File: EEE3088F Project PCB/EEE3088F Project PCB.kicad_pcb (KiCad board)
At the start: 2 copper layers, 80 x 54.9 mm, 76 parts, among them IC1 74LVC1G04SE-7, J1 JST PH 2.00mm connector, SW1 SS-12D10L3, U1 DRV8833PWR, U10 LM7805L-TF3-T, U11 TC4056A., U2 DRV8833PWPR, U3 INA219AxD, U4 CH224K, U6 MIC5504-1.2YM5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

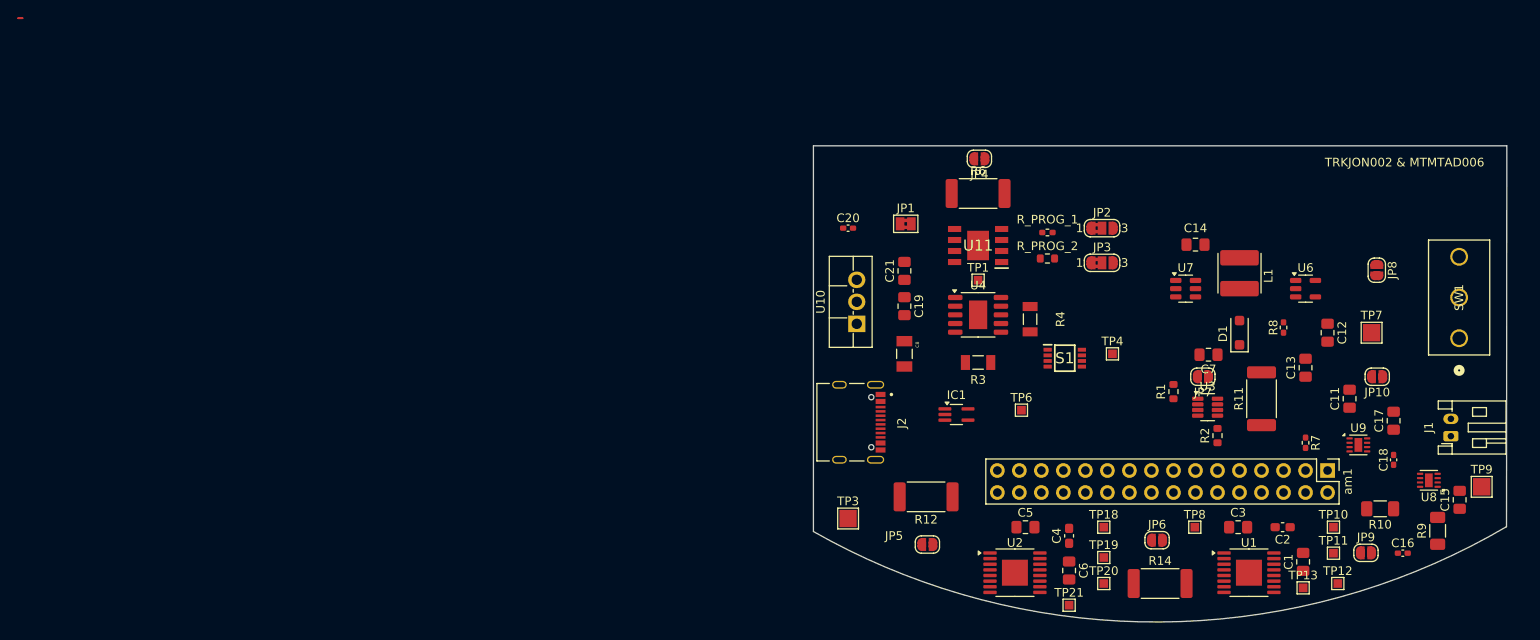
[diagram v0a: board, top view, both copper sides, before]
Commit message: adjusted position of 2*16 connector
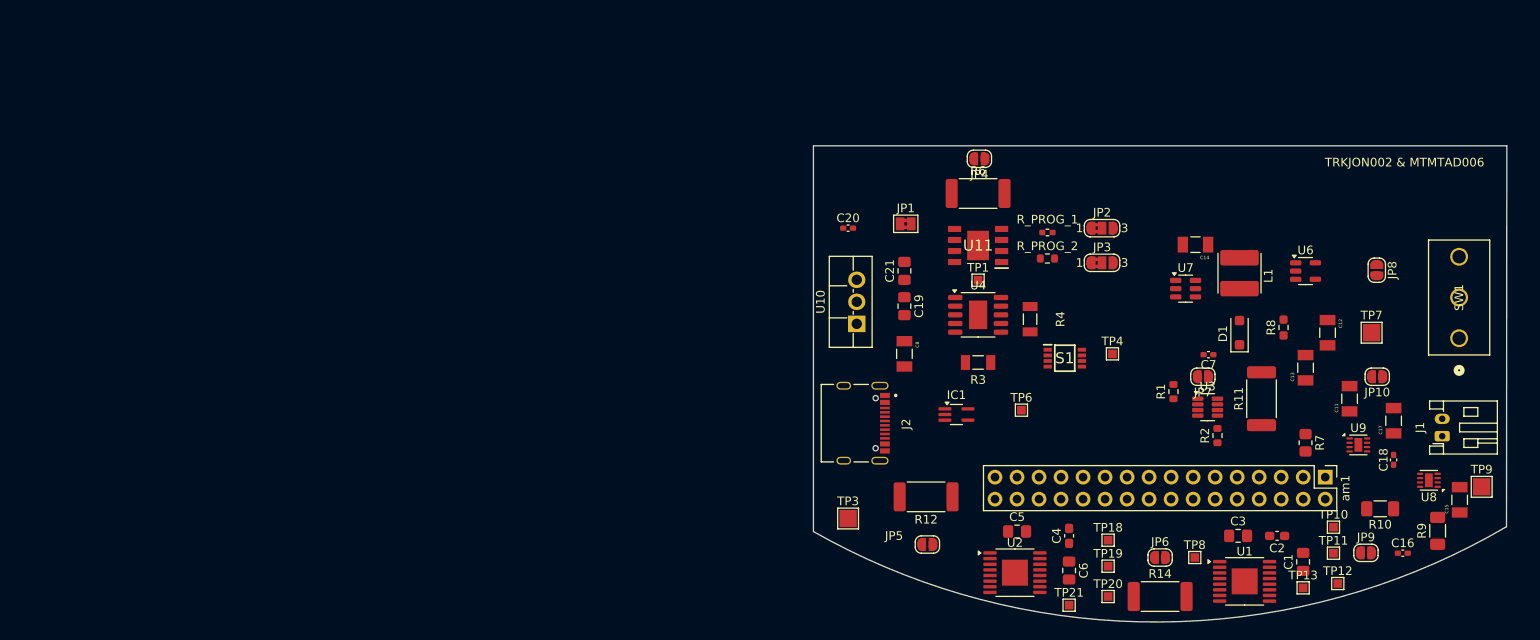
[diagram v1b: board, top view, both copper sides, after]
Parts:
- C11, C12, C13, C14, C15, C17: footprint Capacitor_SMD:C_0805_2012Metric_Pad1.18x1.45mm_HandSolder -> exported_footprints:CAPC3216X180N
- C7: footprint Capacitor_SMD:C_0805_2012Metric_Pad1.18x1.45mm_HandSolder -> Capacitor_SMD:C_0402_1005Metric_Pad0.74x0.62mm_HandSolder
- R7: footprint Resistor_SMD:R_0402_1005Metric_Pad0.72x0.64mm_HandSolder -> Resistor_SMD:R_0805_2012Metric_Pad1.20x1.40mm_HandSolder
- R8: footprint Resistor_SMD:R_0402_1005Metric_Pad0.72x0.64mm_HandSolder -> Resistor_SMD:R_0603_1608Metric_Pad0.98x0.95mm_HandSolder
- moved TP8 3.50 mm to (195.5, 125.0)
- moved JP6 2.03 mm to (191.5, 125.0)
- moved U6 2.03 mm to (208.3, 92.0)
- moved TP18 1.58 mm to (185.5, 123.0)
- moved TP20 1.58 mm to (185.5, 129.5)
- moved R14 1.50 mm to (191.5, 129.5)
- moved C2 1.19 mm to (205.0, 122.5)
- moved TP19 1.12 mm to (185.5, 126.0)
- moved U1 1.12 mm to (201.2, 127.8)
- moved C5 1.08 mm to (175.0, 122.0)
- moved C3 1.00 mm to (200.5, 122.5)
- moved J1 1.00 mm to (224.1, 111.0)
- moved am1 0.81 mm to (210.6, 115.7)
- moved J2 0.51 mm to (155.0, 109.5)

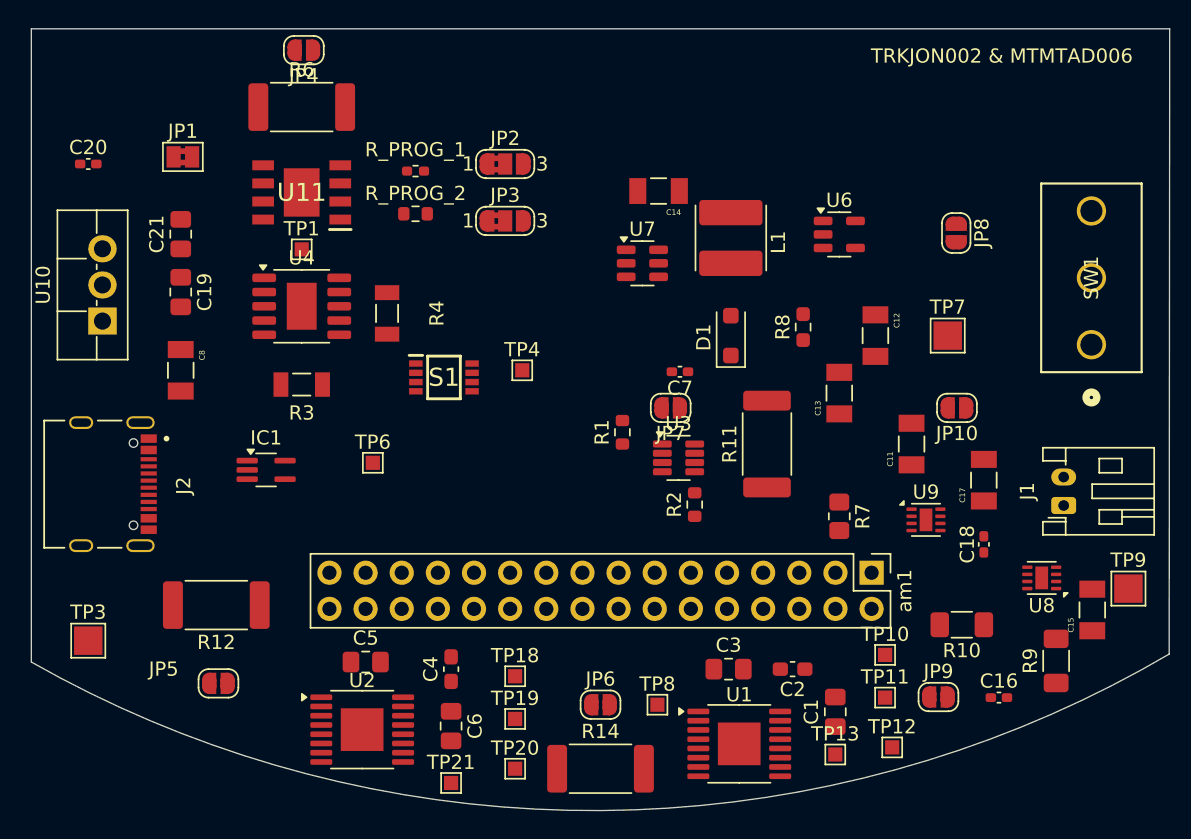
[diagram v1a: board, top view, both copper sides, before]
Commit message: updated the layout of the PCB to better make use of space
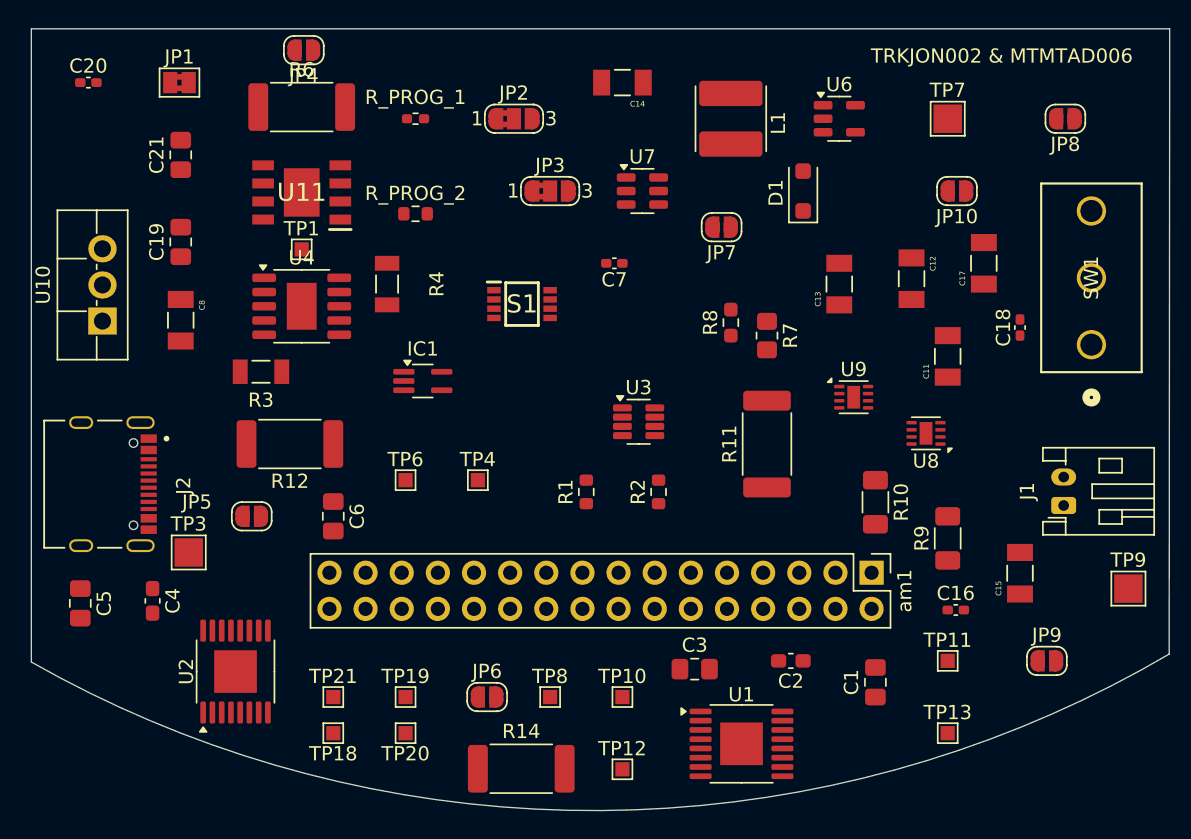
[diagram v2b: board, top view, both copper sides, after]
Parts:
- moved C4 21.5 mm to (160.0, 117.7), turned to -90 degrees
- moved C5 20.5 mm to (154.9, 117.9), turned to -90 degrees
- moved TP12 19.0 mm to (193.0, 129.5)
- moved TP10 18.7 mm to (193.0, 124.5)
- moved C6 16.9 mm to (172.7, 111.8)
- moved C18 15.5 mm to (221.0, 98.5)
- moved TP7 15.2 mm to (215.9, 83.8)
- moved C17 15.2 mm to (218.4, 94.0)
- moved JP10 15.2 mm to (216.6, 88.9)
- moved R7 13.7 mm to (203.2, 99.1)
- moved TP18 13.4 mm to (172.7, 127.0), turned to 180 degrees
- moved JP7 13.2 mm to (200.0, 91.4)
- moved U8 13.0 mm to (214.4, 105.9)
- moved IC1 12.7 mm to (179.0, 102.2)
- moved R12 12.4 mm to (169.7, 106.7)
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
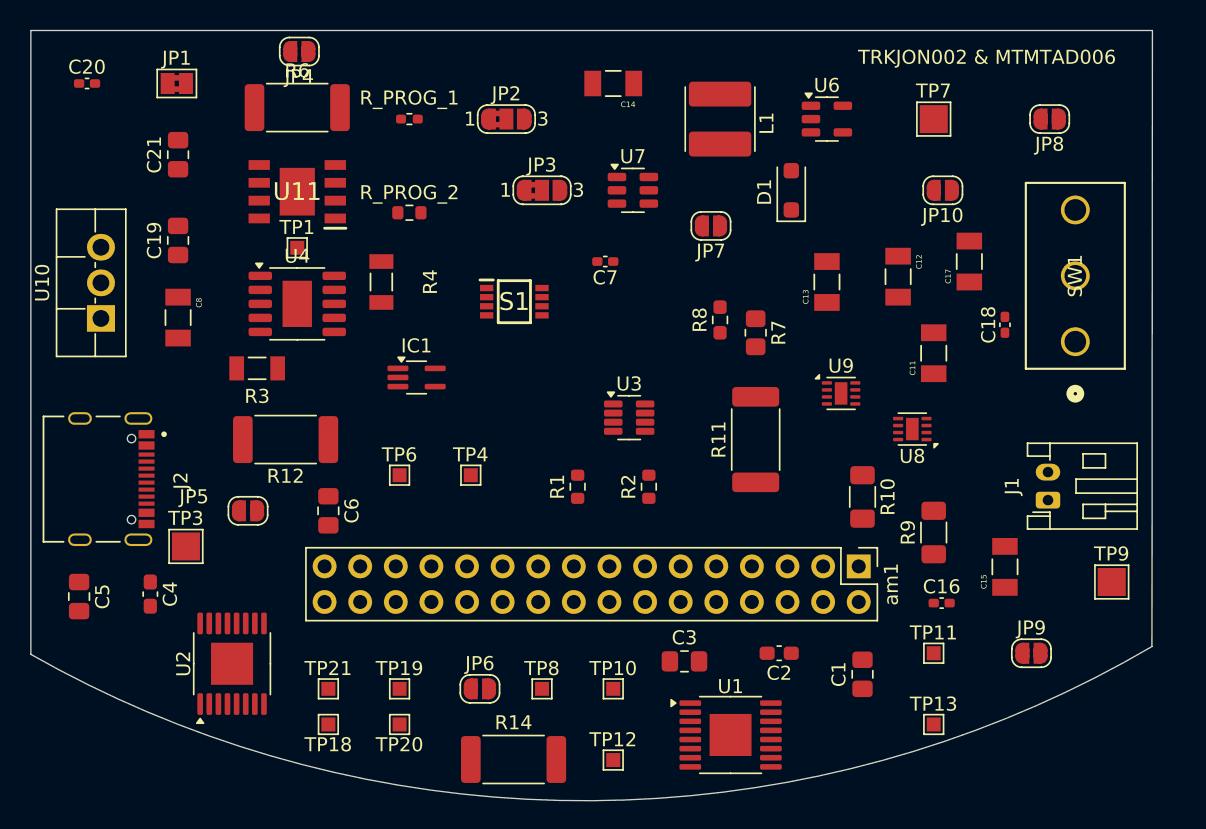
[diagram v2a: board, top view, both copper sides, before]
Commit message: changed inverter IC to a npn inverting switch, assigned new part numbers, added routing with no diameter considerations, added mounting holes,made component designators more visible, added copper fill zone for ground
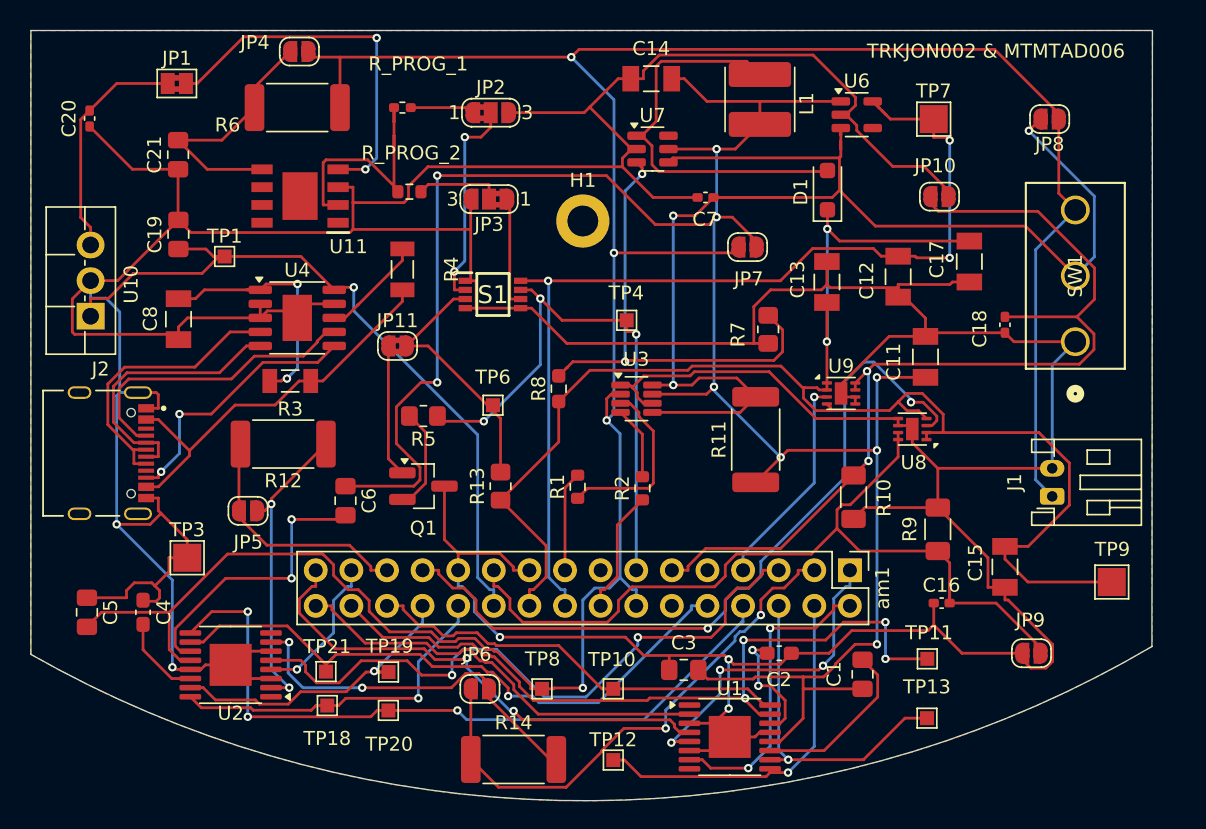
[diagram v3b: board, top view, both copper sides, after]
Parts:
- removed IC1: 74LVC1G04SE-7, Package_TO_SOT_SMD:SOT-353_SC-70-5_Handsoldering
- added H1: MountingHole, MountingHole:MountingHole_2.2mm_M2_DIN965_Pad, F.Cu at (190.9, 91.1)
- added JP11: SolderJumper_2_Bridged, Jumper:SolderJumper-2_P1.3mm_Bridged2Bar_RoundedPad1.0x1.5mm, F.Cu at (177.7, 100.0)
- added Q1: NPN, Package_TO_SOT_SMD:SOT-23_Handsoldering, F.Cu at (179.5, 110.0)
- added R13: 100, Resistor_SMD:R_0805_2012Metric_Pad1.20x1.40mm_HandSolder, F.Cu at (185.0, 110.0)
- added R5: 470, Resistor_SMD:R_0805_2012Metric_Pad1.20x1.40mm_HandSolder, F.Cu at (179.5, 105.0)
- moved TP4 15.7 mm to (194.0, 98.2)
- moved R8 12.5 mm to (189.2, 103.0)
- moved C7 8.48 mm to (199.6, 89.4)
- moved TP6 8.32 mm to (184.5, 104.2)
- moved TP1 5.22 mm to (165.3, 93.6)
- moved JP3 3.83 mm to (184.2, 89.5), turned to 180 degrees
- moved U7 3.26 mm to (195.8, 86.0)
- moved L1 3.17 mm to (203.5, 82.4)
- moved JP7 3.02 mm to (202.6, 93.0)
- moved C14 2.73 mm to (195.8, 80.9)
- moved D1 2.58 mm to (208.3, 88.9)
- moved R3 2.53 mm to (170.0, 102.5)
- moved C20 2.51 mm to (155.7, 83.8), turned to -90 degrees
- moved U6 2.15 mm to (210.4, 83.5)
- moved J2 1.85 mm to (155.0, 107.7)
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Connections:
- net Net-(IC1-Y) renamed /2E
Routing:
- net GND: track 0.00 -> 440.6 mm, vias 0 -> 5
- net /Battery: track 0.00 -> 200.4 mm, vias 0 -> 4
- net /V_sensing: track 0.00 -> 162.9 mm, vias 0 -> 9
- net /5V Out: track 0.00 -> 111.5 mm, vias 0 -> 2
- net /V_switch: track 0.00 -> 98.1 mm, vias 0 -> 3
- net /3V3 Out: track 0.00 -> 72.6 mm, vias 0 -> 3
- net /EXT_LOAD2_OUT: track 0.00 -> 68.5 mm, vias 0 -> 2
- net /EXT_LOAD1_OUT: track 0.00 -> 61.4 mm
- net /CTRL_EXT_LOAD1: track 0.00 -> 54.9 mm, vias 0 -> 2
- net /MOTOR1_CTRL2: track 0.00 -> 54.1 mm, vias 0 -> 4
- net /HV: track 0.00 -> 52.6 mm, vias 0 -> 1
- net /MOTOR4_CTRL1: track 0.00 -> 52.1 mm, vias 0 -> 3
- net /Motor4_B_OUT: track 0.00 -> 46.2 mm, vias 0 -> 2
- net /MOTOR4_CTRL2: track 0.00 -> 44.1 mm, vias 0 -> 1
- net /FAST_CHARGE_CTRL: track 0.00 -> 40.7 mm, vias 0 -> 3
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- added copper zone on F.Cu, net GND

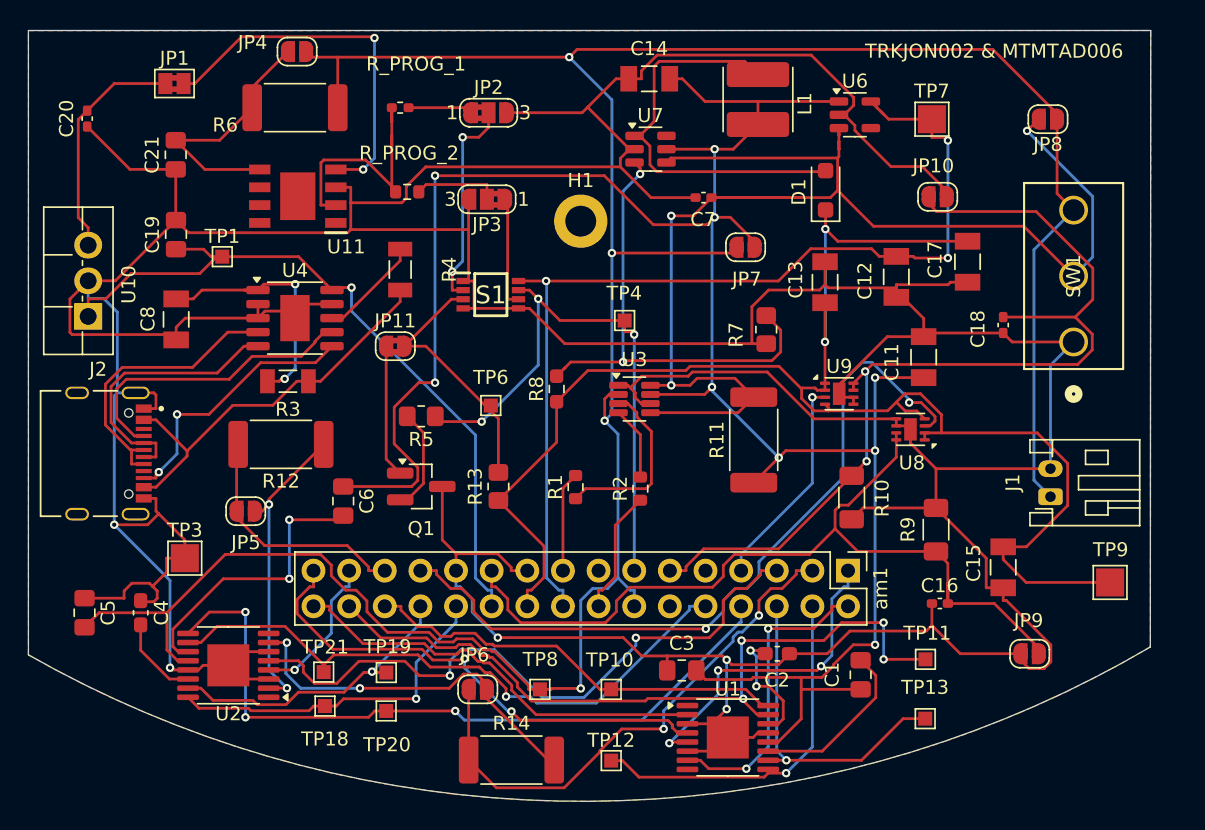
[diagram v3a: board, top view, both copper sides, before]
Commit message: completed the first iteration where all routing is completed
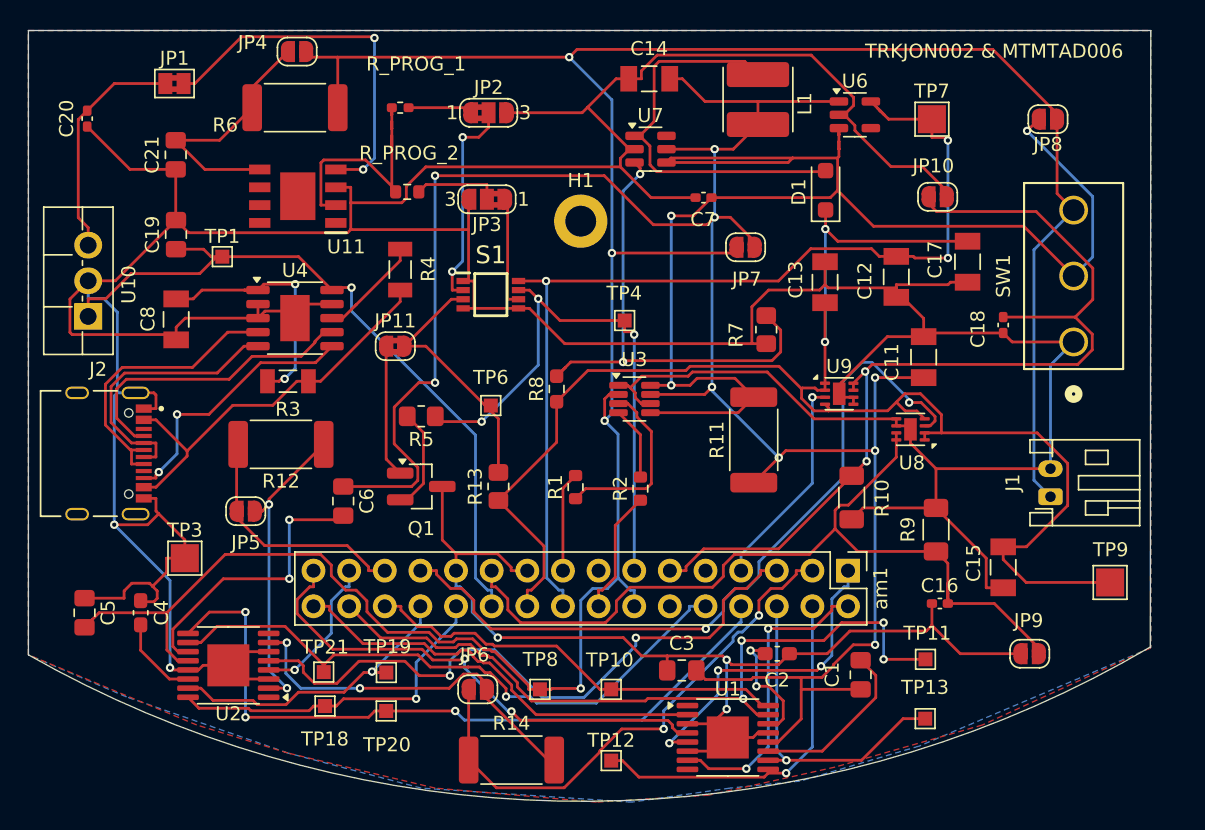
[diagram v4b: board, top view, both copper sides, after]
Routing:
- net GND: track 440.6 -> 431.1 mm
- net /V_switch: track 98.1 -> 100.7 mm
- added copper zone on B.Cu, net /Battery

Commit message: competed half my routing adjustments and removed DRC errors, noted a pproblem with the Q1 symbol
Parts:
- moved TP1 1.18 mm to (166.5, 93.6)
- moved C20 0.42 mm to (156.0, 83.5)
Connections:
- C5 pad 2: /Battery -> /V_sensing
- U2 pad 12: /Battery -> /V_sensing
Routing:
- net GND: track 431.1 -> 286.4 mm, vias 5 -> 8
- net /V_sensing: track 162.7 -> 208.6 mm
- net /Battery: track 200.1 -> 154.8 mm
- net /EXT_LOAD2_OUT: track 68.5 -> 72.1 mm
- net /VBUS: track 28.8 -> 30.7 mm
- net Net-(JP11-A): track 9.46 -> 10.7 mm
